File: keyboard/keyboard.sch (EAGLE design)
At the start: 32 parts, among them SW1 CHERRY_MX, SW10 CHERRY_MX, SW11 CHERRY_MX, SW12 CHERRY_MX, SW13 CHERRY_MX, SW14 CHERRY_MX, SW15 CHERRY_MX, SW16 CHERRY_MX, SW17 CHERRY_MX, SW18 CHERRY_MX, SW19 CHERRY_MX, SW2 CHERRY_MX, SW20 CHERRY_MX, SW21 CHERRY_MX, SW22 CHERRY_MX, SW23 CHERRY_MX, SW24 CHERRY_MX, SW25 CHERRY_MX, SW26 CHERRY_MX, SW27 CHERRY_MX, SW28 CHERRY_MX, SW3 CHERRY_MX, SW4 CHERRY_MX, SW5 CHERRY_MX, SW6 CHERRY_MX, SW7 CHERRY_MX, SW8 CHERRY_MX, SW9 CHERRY_MX

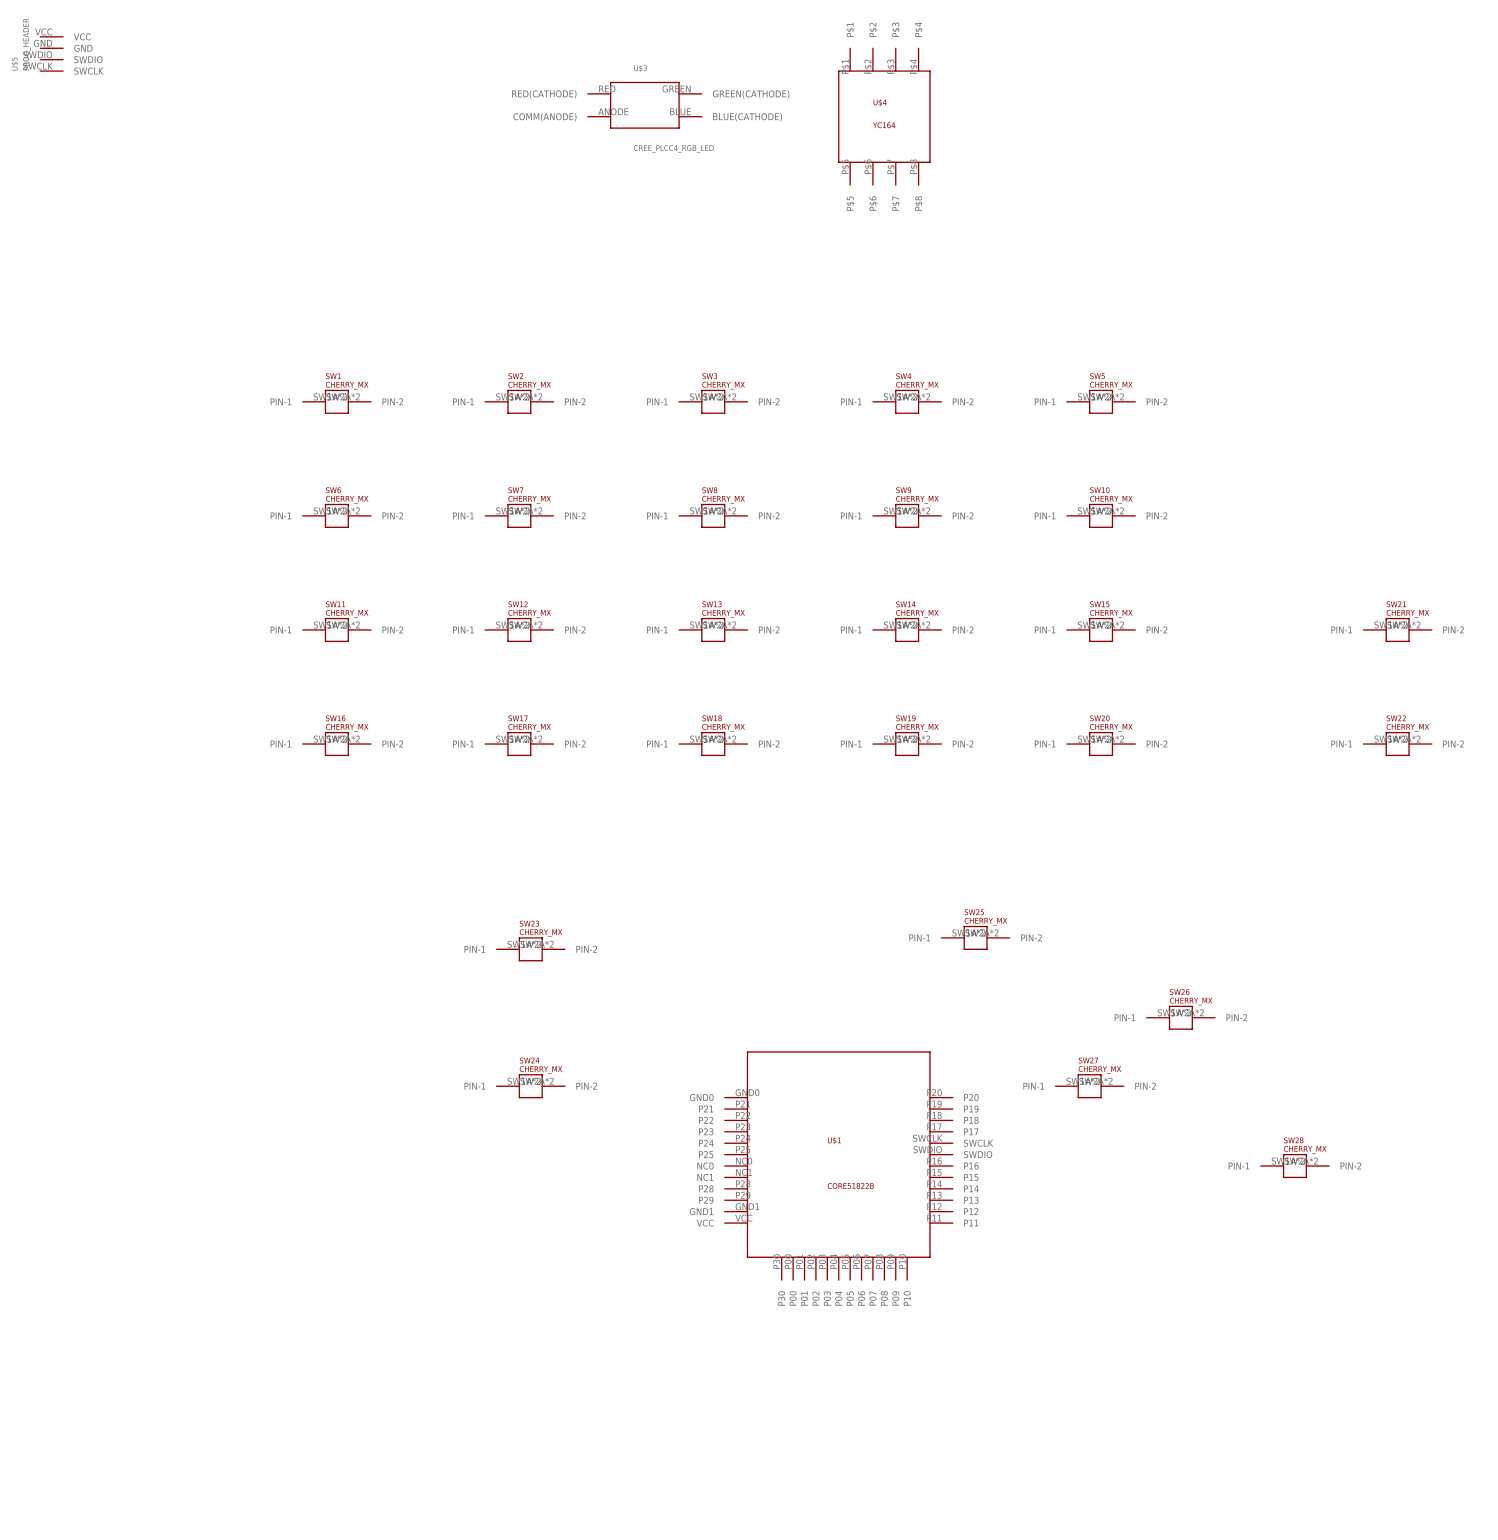
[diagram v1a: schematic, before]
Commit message: wire up switches
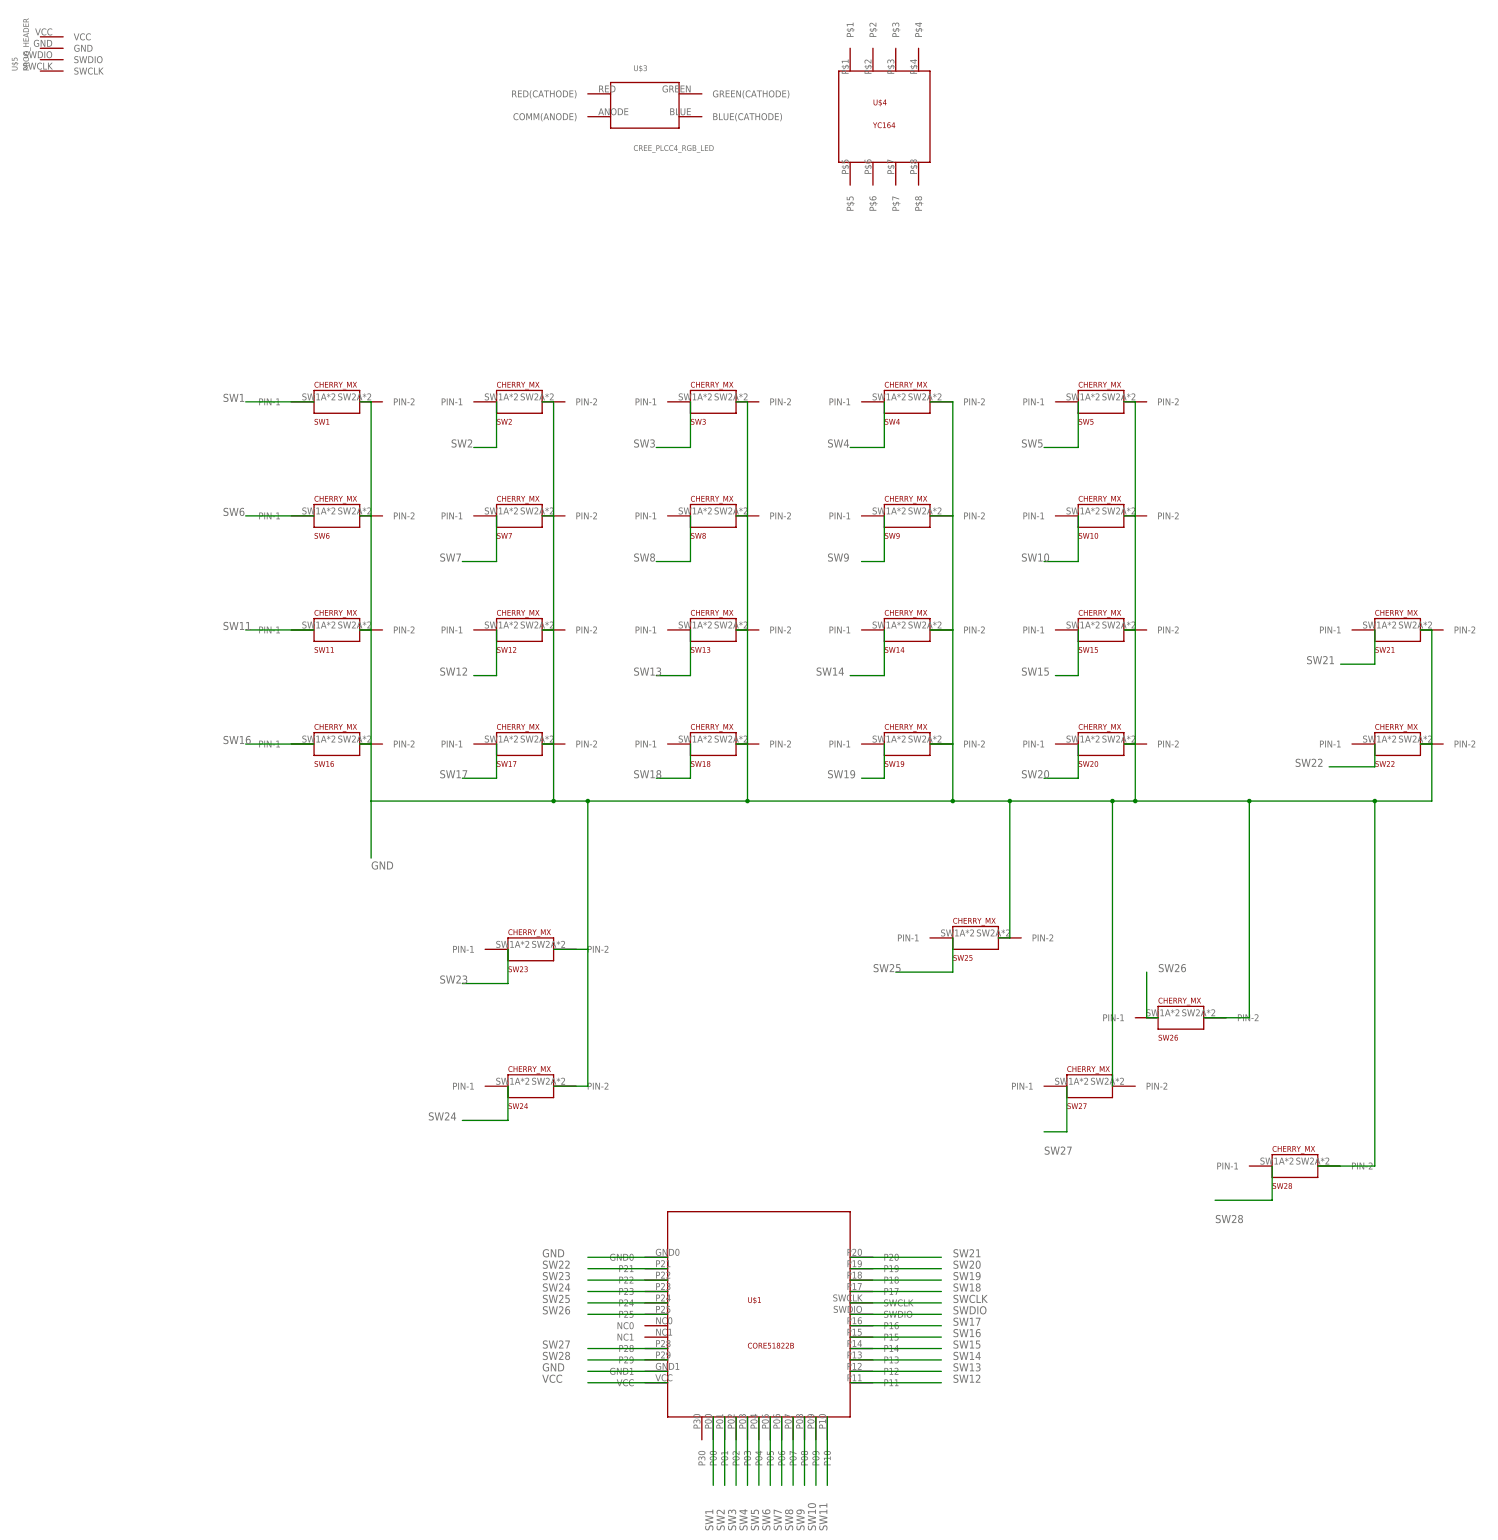
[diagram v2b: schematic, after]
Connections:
- new net GND: SW1.PIN-2, SW10.PIN-2, SW11.PIN-2, SW12.PIN-2, SW13.PIN-2, SW14.PIN-2, SW15.PIN-2, SW16.PIN-2, SW17.PIN-2, SW18.PIN-2, SW19.PIN-2, SW2.PIN-2, SW20.PIN-2, SW21.PIN-2, SW22.PIN-2, SW23.PIN-2, SW24.PIN-2, SW25.PIN-2, SW26.PIN-2, SW27.PIN-2, SW28.PIN-2, SW3.PIN-2, SW4.PIN-2, SW5.PIN-2, SW6.PIN-2, SW7.PIN-2, SW8.PIN-2, SW9.PIN-2, U$1.GND0, U$1.GND1
- new net SW1: SW1.PIN-1, U$1.P00
- new net SW10: SW10.PIN-1, U$1.P09
- new net SW11: SW11.PIN-1, U$1.P10
- new net SW12: SW12.PIN-1, U$1.P11
- new net SW13: SW13.PIN-1, U$1.P12
- new net SW14: SW14.PIN-1, U$1.P13
- new net SW15: SW15.PIN-1, U$1.P14
- new net SW16: SW16.PIN-1, U$1.P15
- new net SW17: SW17.PIN-1, U$1.P16
- new net SW18: SW18.PIN-1, U$1.P17
- new net SW19: SW19.PIN-1, U$1.P18
- new net SW2: SW2.PIN-1, U$1.P01
- new net SW20: SW20.PIN-1, U$1.P19
- new net SW21: SW21.PIN-1, U$1.P20
- new net SW22: SW22.PIN-1, U$1.P21
- new net SW23: SW23.PIN-1, U$1.P22
- new net SW24: SW24.PIN-1, U$1.P23
- new net SW25: SW25.PIN-1, U$1.P24
- new net SW26: SW26.PIN-1, U$1.P25
- new net SW27: SW27.PIN-1, U$1.P28
- new net SW28: SW28.PIN-1, U$1.P29
- new net SW3: SW3.PIN-1, U$1.P02
- new net SW4: SW4.PIN-1, U$1.P03
- new net SW5: SW5.PIN-1, U$1.P04
- new net SW6: SW6.PIN-1, U$1.P05
- new net SW7: SW7.PIN-1, U$1.P06
- new net SW8: SW8.PIN-1, U$1.P07
- new net SW9: SW9.PIN-1, U$1.P08
- new net SWCLK: U$1.SWCLK
- new net SWDIO: U$1.SWDIO
- new net VCC: U$1.VCC
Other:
- moved on the sheet: U$1

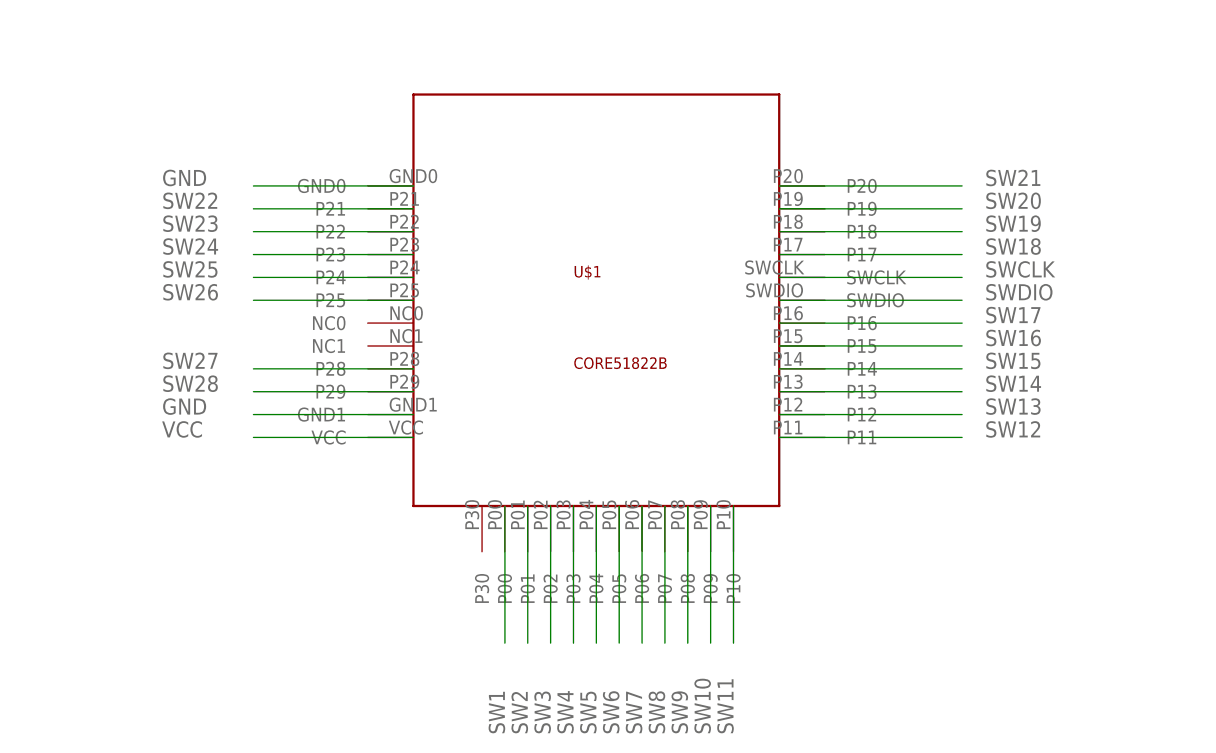
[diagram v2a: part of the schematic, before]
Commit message: rearrange pins to eliminate vias
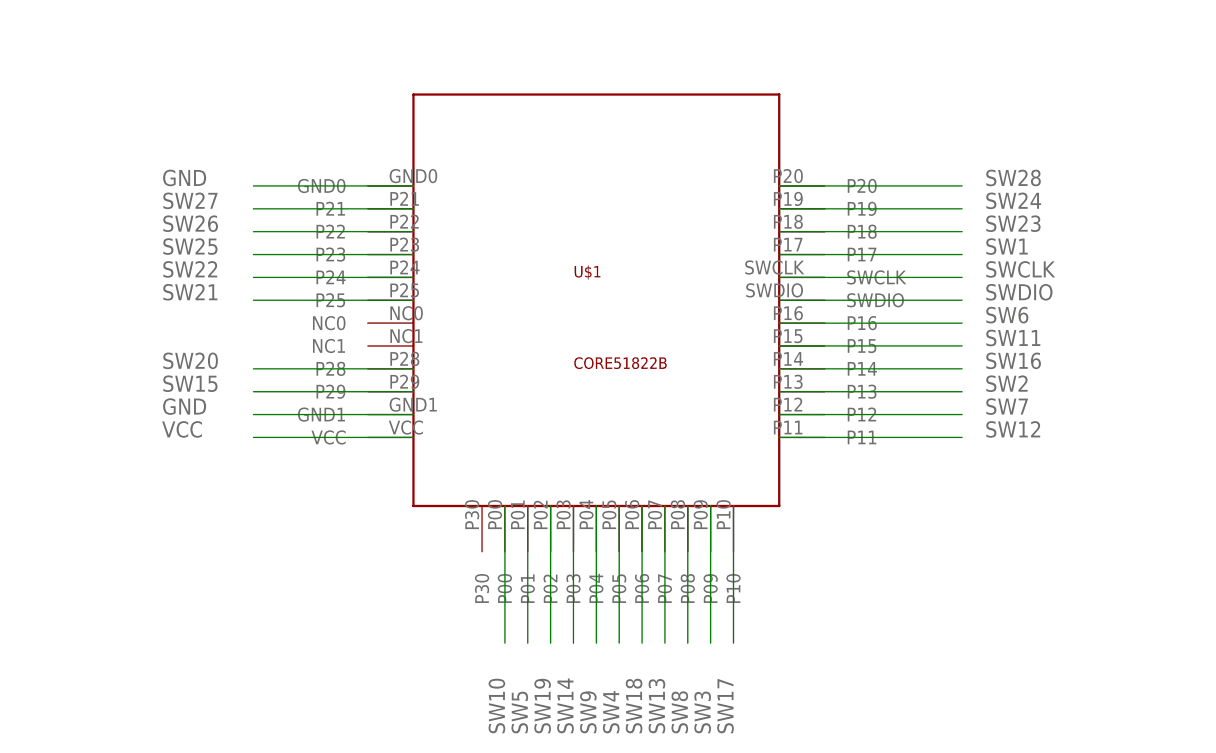
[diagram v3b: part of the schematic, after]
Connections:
- net SW1: now also U$1.P17; no longer U$1.P00
- net SW10: now also U$1.P00; no longer U$1.P09
- net SW11: now also U$1.P15; no longer U$1.P10
- net SW13: now also U$1.P07; no longer U$1.P12
- net SW14: now also U$1.P03; no longer U$1.P13
- net SW15: now also U$1.P29; no longer U$1.P14
- net SW16: now also U$1.P14; no longer U$1.P15
- net SW17: now also U$1.P10; no longer U$1.P16
- net SW18: now also U$1.P06; no longer U$1.P17
- net SW19: now also U$1.P02; no longer U$1.P18
- net SW2: now also U$1.P13; no longer U$1.P01
- net SW20: now also U$1.P28; no longer U$1.P19
- net SW21: now also U$1.P25; no longer U$1.P20
- net SW22: now also U$1.P24; no longer U$1.P21
- net SW23: now also U$1.P18; no longer U$1.P22
- net SW24: now also U$1.P19; no longer U$1.P23
- net SW25: now also U$1.P23; no longer U$1.P24
- net SW26: now also U$1.P22; no longer U$1.P25
- net SW27: now also U$1.P21; no longer U$1.P28
- net SW28: now also U$1.P20; no longer U$1.P29
- net SW3: now also U$1.P09; no longer U$1.P02
- net SW4: now also U$1.P05; no longer U$1.P03
- net SW5: now also U$1.P01; no longer U$1.P04
- net SW6: now also U$1.P16; no longer U$1.P05
- net SW7: now also U$1.P12; no longer U$1.P06
- net SW8: now also U$1.P08; no longer U$1.P07
- net SW9: now also U$1.P04; no longer U$1.P08

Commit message: consistently align keys
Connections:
- net GND: now also U$5.GND
- net SWCLK: now also U$5.SWCLK
- net SWDIO: now also U$5.SWDIO
- net VCC: now also U$5.VCC
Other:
- moved on the sheet: U$5
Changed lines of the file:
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@@
 <instance part="U$3" gate="G$1" x="99.06" y="30.48"/>
 <instance part="U$4" gate="G$1" x="152.4" y="27.94"/>
-<instance part="U$5" gate="G$1" x="-35.56" y="45.72"/>
+<instance part="U$5" gate="G$1" x="210.82" y="25.4"/>
 <instance part="SW1" gate="G$1" x="30.48" y="-35.56"/>
 <instance part="SW2" gate="G$1" x="71.12" y="-35.56"/>
@@
 <label x="76.2" y="-251.46" size="1.778" layer="95"/>
 </segment>
+<segment>
+<pinref part="U$5" gate="G$1" pin="GND"/>
+<wire x1="210.82" y1="22.86" x2="233.68" y2="22.86" width="0.1524" layer="91"/>
+<label x="236.22" y="22.86" size="1.778" layer="95"/>
+</segment>
 </net>
 <net name="SW1" class="0">
@@
 <label x="167.64" y="-238.76" size="1.778" layer="95"/>
 </segment>
+<segment>
+<pinref part="U$5" gate="G$1" pin="SWDIO"/>
+<wire x1="210.82" y1="20.32" x2="233.68" y2="20.32" width="0.1524" layer="91"/>
+<label x="236.22" y="20.32" size="1.778" layer="95"/>
+</segment>
 </net>
 <net name="SWCLK" class="0">
@@
 <label x="167.64" y="-236.22" size="1.778" layer="95"/>
 </segment>
+<segment>
+<pinref part="U$5" gate="G$1" pin="SWCLK"/>
+<wire x1="210.82" y1="17.78" x2="233.68" y2="17.78" width="0.1524" layer="91"/>
+<label x="236.22" y="17.78" size="1.778" layer="95"/>
+</segment>
 </net>
 <net name="VCC" class="0">
@@
 <label x="76.2" y="-254" size="1.778" layer="95"/>
 </segment>
-</net>
+<segment>
+<pinref part="U$5" gate="G$1" pin="VCC"/>
+<wire x1="210.82" y1="25.4" x2="233.68" y2="25.4" width="0.1524" layer="91"/>
+<label x="236.22" y="25.4" size="1.778" layer="95"/>
+</segment>
+</net>

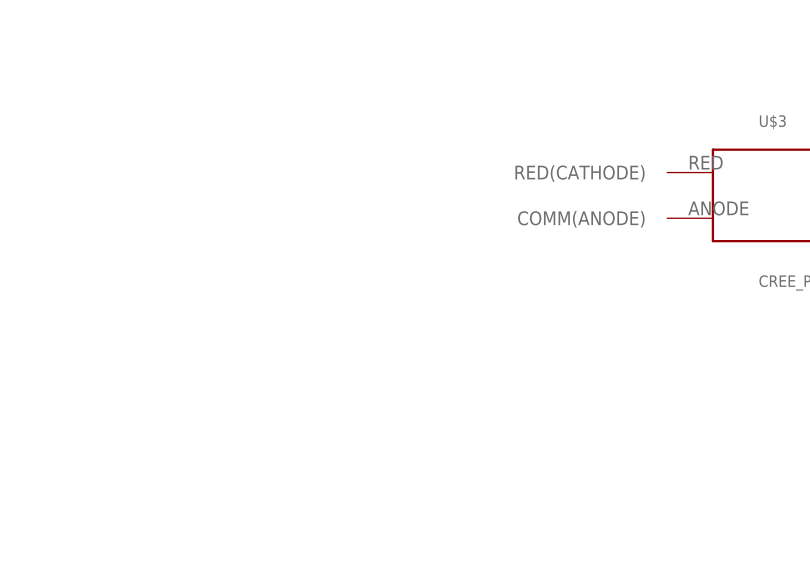
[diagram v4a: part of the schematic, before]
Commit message: add MCP73831T LiPo CMC
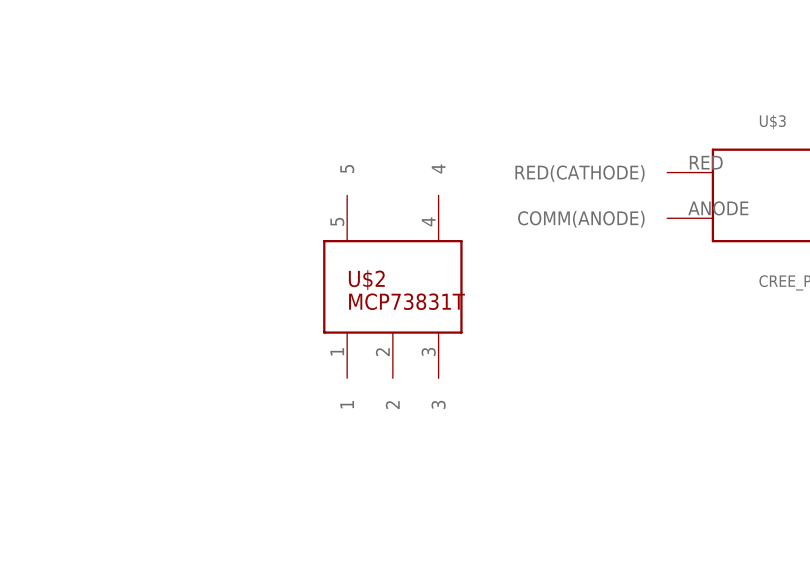
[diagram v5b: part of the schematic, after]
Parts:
- added U$2: MCP73831T, mcp73831t:MCP73831T
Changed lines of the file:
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@@
 <layers>
 <layer number="1" name="Top" color="4" fill="1" visible="no" active="no"/>
+<layer number="2" name="Route2" color="1" fill="3" visible="no" active="no"/>
+<layer number="15" name="Route15" color="4" fill="6" visible="no" active="no"/>
 <layer number="16" name="Bottom" color="1" fill="1" visible="no" active="no"/>
 <layer number="17" name="Pads" color="2" fill="1" visible="no" active="no"/>
@@
 <part name="SW27" library="cherry_mx" deviceset="CHERRY_MX" device=""/>
 <part name="SW28" library="cherry_mx" deviceset="CHERRY_MX" device=""/>
+<part name="U$2" library="mcp73831t" deviceset="MCP73831T" device=""/>
 </parts>
 <sheets>
@@
 <instance part="SW27" gate="G$1" x="198.12" y="-187.96"/>
 <instance part="SW28" gate="G$1" x="243.84" y="-205.74"/>
+<instance part="U$2" gate="G$1" x="55.88" y="20.32"/>
 </instances>
 <busses>
